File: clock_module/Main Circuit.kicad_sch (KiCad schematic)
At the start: 1 part, among them U2 NE555DR

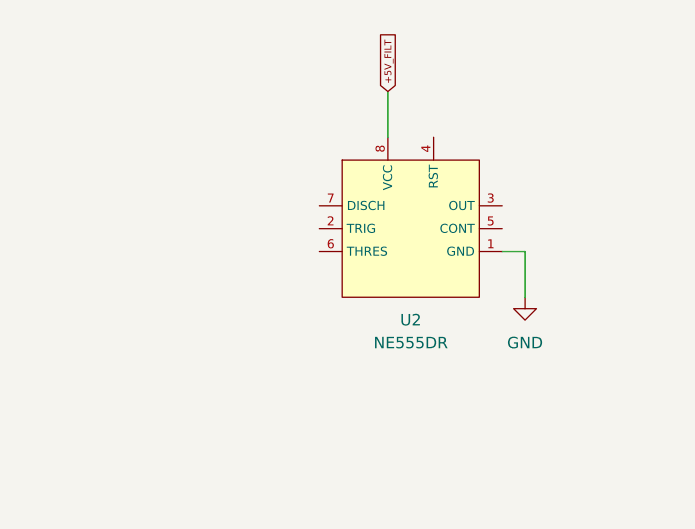
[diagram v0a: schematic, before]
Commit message: add: monostable operation circuit
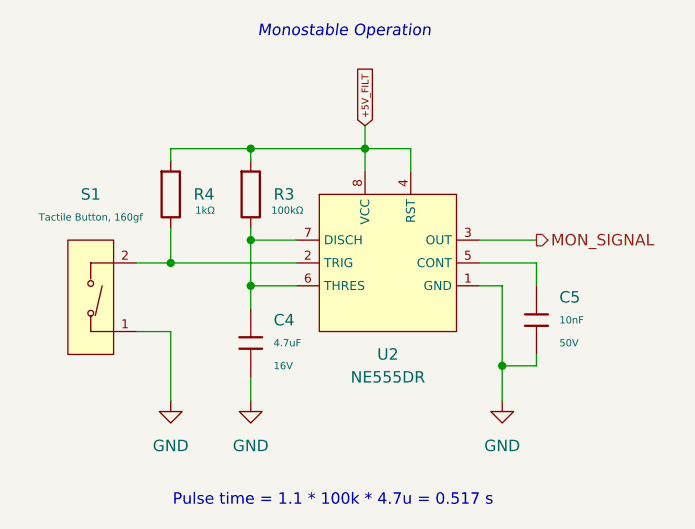
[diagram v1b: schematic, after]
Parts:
- added C4: 4.7uF, PCM_JLCPCB:C_0603, symbol PCM_JLCPCB-Capacitors:0603,4.7uF
- added C5: 10nF, PCM_JLCPCB:C_0603, symbol PCM_JLCPCB-Capacitors:0603,10nF
- added R3: 100kΩ, PCM_JLCPCB:R_0603, symbol PCM_JLCPCB-Resistors:0603,100kΩ
- added R4: 1kΩ, PCM_JLCPCB:R_0603, symbol PCM_JLCPCB-Resistors:0603,1kΩ
- added S1: Tactile Button, 160gf, PCM_JLCPCB:SW_TS-1088-AR02016, symbol PCM_JLCPCB-Connectors_Buttons:Tactile Button, 160gf, 12V, 50mA, 4.0mm
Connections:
- net +5V_FILT: now also U2.4 (RST), R3.1, R4.1
- net GND: now also C4.2, C5.2, S1.1 (A)
- net at U2.2 (TRIG): now also R4.2, S1.2 (B)
- net MON_SIGNAL: now reaches U2.3 (OUT)
- net at U2.5 (CONT): now also C5.1
- net at U2.6 (THRES): now also U2.7 (DISCH), C4.1, R3.2
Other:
- note added: "Monostable Operation"
- note added: "Pulse time = 1.1 * 100k * 4.7u = 0.517 s"
- moved on the sheet: U2

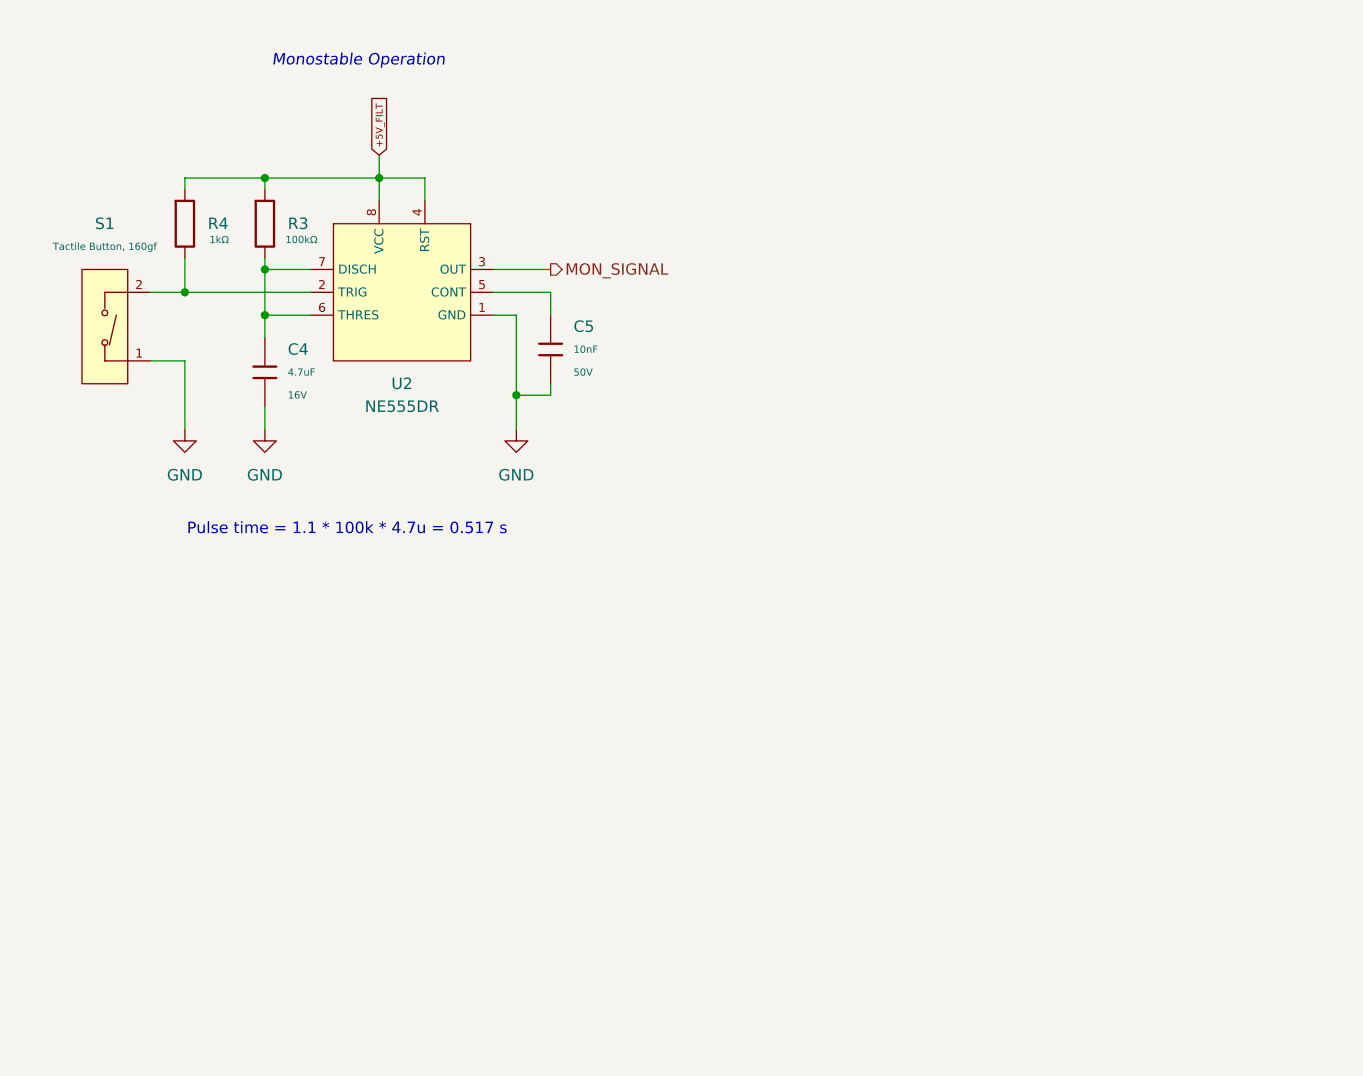
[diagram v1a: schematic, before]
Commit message: add: astable circuit
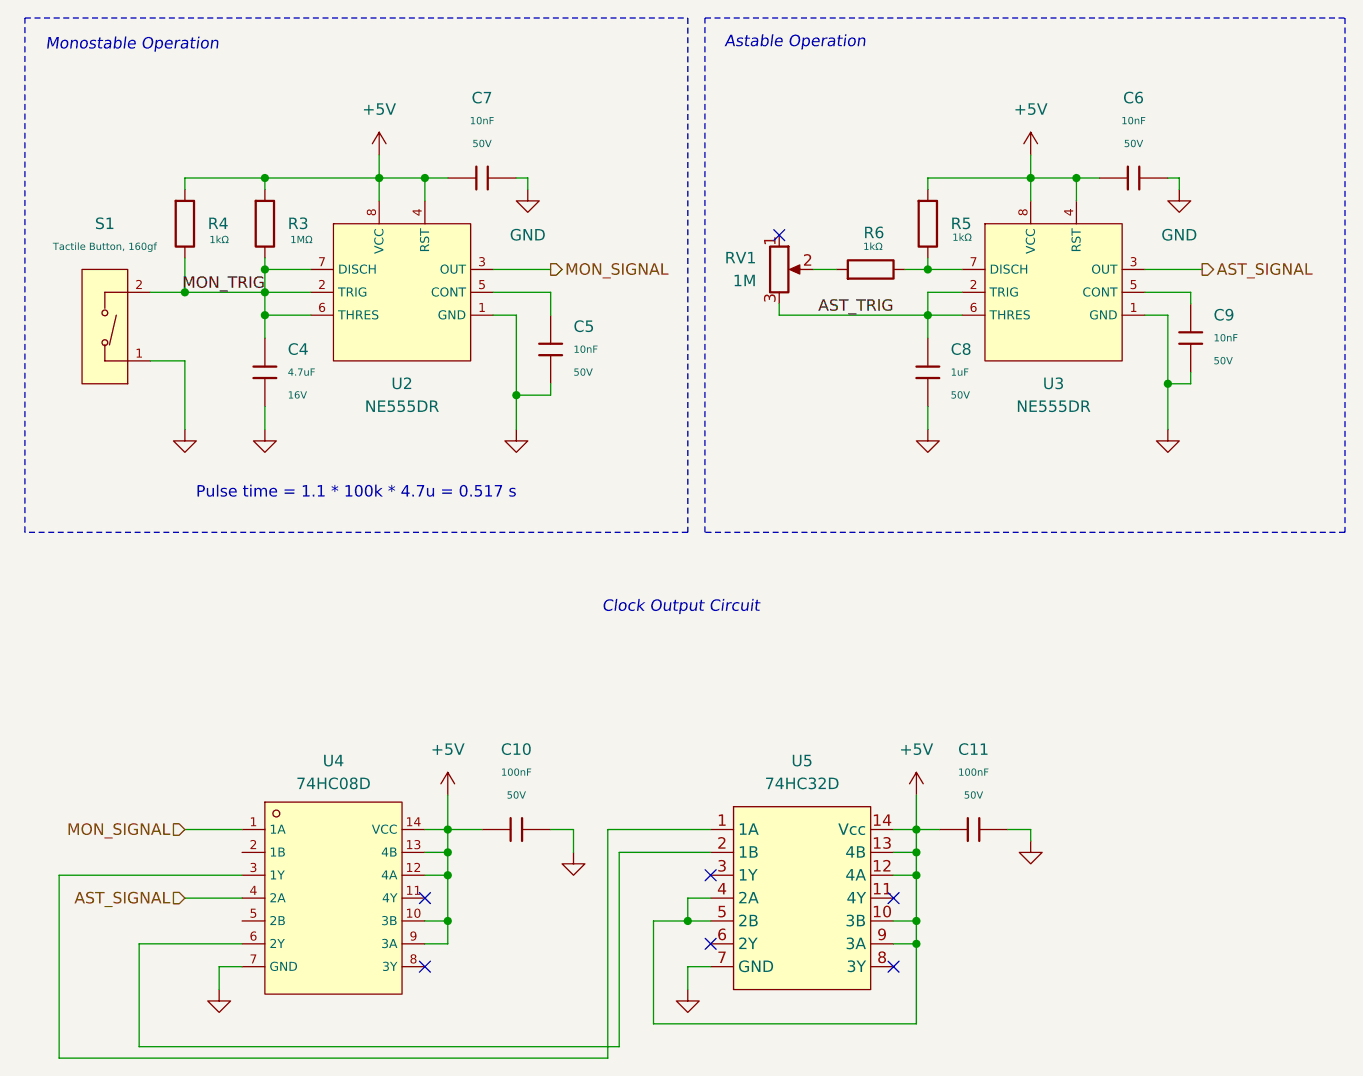
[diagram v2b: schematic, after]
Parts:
- removed R3: 100kΩ, PCM_JLCPCB:R_0603, symbol PCM_JLCPCB-Resistors:0603,100kΩ
- added C10, C11: 100nF, PCM_JLCPCB:C_0603, symbol PCM_JLCPCB-Capacitors:0603,100nF
- added C6, C7, C9: 10nF, PCM_JLCPCB:C_0603, symbol PCM_JLCPCB-Capacitors:0603,10nF
- added C8: 1uF, PCM_JLCPCB:C_0603, symbol PCM_JLCPCB-Capacitors:0603,1uF
- added R3: 1MΩ, PCM_JLCPCB:R_0603, symbol PCM_JLCPCB-Resistors:0603,1MΩ
- added R5, R6: 1kΩ, PCM_JLCPCB:R_0603, symbol PCM_JLCPCB-Resistors:0603,1kΩ
- added RV1: 1M, Potentiometer_SMD:Potentiometer_Bourns_3314G_Vertical, symbol Device:R_Potentiometer
- added U3: NE555DR, PCM_JLCPCB:SOIC-8_L4.9-W3.9-P1.27-LS6.0-BL, symbol PCM_JLCPCB-ICs:Timer, 555
- added U4: 74HC08D, PCM_JLCPCB:SOIC-14_L8.7-W3.9-P1.27-LS6.0-BL, symbol PCM_JLCPCB-ICs:Gate, AND, 4 Channel, 74HC08D,653
- added U5: 74HC32D, PCM_JLCPCB:SOIC-14_L8.7-W3.9-P1.27-LS6.0-BL, symbol PCM_JLCPCB-ICs:Gate,_OR,_4_Channel,_74HC32D,653
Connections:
- net GND: now also C10.2, C11.2, C6.2, C7.2, C8.2, C9.2, U3.1 (GND), U4.7 (GND), U5.7 (GND)
- net MON_SIGNAL: now also U4.1 (1A)
- net MON_TRIG: now reaches C4.1, U2.6 (THRES), U2.7 (DISCH)
- net MON_TRIG: now also R4.2, S1.2 (B), U2.2 (TRIG), R3.2
- net +5V_FILT renamed +5V
- net +5V: now also C10.1, C11.1, C6.1, C7.1, R3.1, R5.1, U3.4 (RST), U3.8 (VCC), U4.10 (3B), U4.12 (4A), U4.13 (4B), U4.14 (VCC), U4.9 (3A), U5.10 (3B), U5.12 (4A), U5.13 (4B), U5.14 (Vcc), U5.4 (2A), U5.5 (2B), U5.9 (3A)
- new net: C9.1, U3.5 (CONT)
- new net: R5.2, R6.2, U3.7 (DISCH)
- new net: U4.3 (1Y), U5.1 (1A)
- new net: U4.6 (2Y), U5.2 (1B)
- new net: R6.1, RV1.2
- new net AST_SIGNAL: U3.3 (OUT), U4.4 (2A)
- new net AST_TRIG: C8.1, RV1.3, U3.2 (TRIG), U3.6 (THRES)
- no-connect marks 0 -> 7
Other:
- note added: "Astable Operation"
- note added: "Clock Output Circuit"

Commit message: pcb routes (unfinished)
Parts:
- added C12, C13: 10nF, PCM_JLCPCB:C_0603, symbol PCM_JLCPCB-Capacitors:0603,10nF
- added C14: 100nF, PCM_JLCPCB:C_0603, symbol PCM_JLCPCB-Capacitors:0603,100nF
- added D1: Yellow, PCM_JLCPCB:D_0603, symbol PCM_JLCPCB-Diodes:LED,0603,Yellow
- added J2: Conn_01x03, Connector_PinHeader_2.54mm:PinHeader_1x03_P2.54mm_Vertical, symbol Connector_Generic:Conn_01x03
- added R7: 220Ω, PCM_JLCPCB:R_0603, symbol PCM_JLCPCB-Resistors:0603,220Ω
- added R8, R9: 1kΩ, PCM_JLCPCB:R_0603, symbol PCM_JLCPCB-Resistors:0603,1kΩ
- added SW1: SW_SPDT, Buttons_THT:SW_SPDT_L7.0mm_H16.0mm_W7.00mm, symbol Switch:SW_SPDT
- added U6: NE555DR, PCM_JLCPCB:SOIC-8_L4.9-W3.9-P1.27-LS6.0-BL, symbol PCM_JLCPCB-ICs:Timer, 555
- added U7: 74HC04D, PCM_JLCPCB:SOIC-14_L8.7-W3.9-P1.27-LS6.0-BL, symbol PCM_JLCPCB-ICs:Inverter, 6 Channel, 74HC04D,653
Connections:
- net +5V: now also C12.1, C14.1, R8.1, R9.1, U6.8 (VCC), U7.11 (5A), U7.13 (6A), U7.14 (VCC), U7.9 (4A); no longer U4.10 (3B), U4.9 (3A)
- net GND: now also C12.2, C13.2, C14.2, R7.1, SW1.2 (B), U6.1 (GND), U6.6 (THRES), U7.7 (GND)
- net SIG_SELECT: now reaches U4.2 (1B)
- net SIG_SELECT: now also U6.3 (OUT), U7.1 (1A)
- net !SIG_SELECT: now reaches U4.5 (2B)
- net !SIG_SELECT: now also U7.2 (1Y)
- net CLK_SIGNAL: now reaches U4.8 (3Y)
- net CLK_SIGNAL: now also D1.2, J2.2 (Pin_2), U7.5 (3A)
- net at U5.3 (1Y): now also U4.10 (3B)
- new net: C13.1, U6.5 (CONT)
- new net: U4.9 (3A), U7.4 (2Y)
- new net: R8.2, SW1.1 (A), U6.2 (TRIG)
- new net: R9.2, SW1.3 (C), U6.4 (RST)
- new net: D1.1, R7.2
- new net !CLK_SIGNAL: J2.3 (Pin_3), U7.6 (3Y)
- new net HLT: J2.1 (Pin_1), U7.3 (2A)
- no-connect marks 7 -> 9
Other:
- note added: "!CLK - Inverted Clock Signal"
- note added: "Bistable Operation"
- note added: "CLK - Clock Signal"
- note added: "HLT - From Controller Circuit"
- note added: "Input/Output Headers"
- note added: "Pulse time = 1.1 * 1M * 4.7u = 5.17 s"
- note removed: "Pulse time = 1.1 * 100k * 4.7u = 0.517 s"
- moved on the sheet: C6, C8, C9, R5, R6, RV1, U3

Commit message: finished board
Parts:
- RV1: LCSC (none) -> C780218
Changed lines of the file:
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@@
+			)
+		)
+		(property "LCSC" "C780218"
+			(at 110.49 45.72 0)
+			(effects
+				(font
+					(size 1.27 1.27)
+				)
+				(hide yes)
 			)
 		)

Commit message: final v1.0.0 project
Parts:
- removed J2: Conn_01x03, Connector_PinHeader_2.54mm:PinHeader_1x03_P2.54mm_Vertical, symbol Connector_Generic:Conn_01x03
- removed R6: 1kΩ, PCM_JLCPCB:R_0603, symbol PCM_JLCPCB-Resistors:0603,1kΩ
- added J3: Conn_01x05, Connector_PinHeader_2.54mm:PinHeader_1x05_P2.54mm_Vertical, symbol Connector_Generic:Conn_01x05
- added R6: 200kΩ, PCM_JLCPCB:R_0603, symbol PCM_JLCPCB-Resistors:0603,200kΩ
- RV1: value 1M -> 200k; LCSC C780218 -> C3345207
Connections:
- net !CLK_SIGNAL: now also J3.3 (Pin_3)
- net +5V: now also J3.4 (Pin_4)
- net CLK_SIGNAL: now also J3.2 (Pin_2)
- net GND: now also J3.5 (Pin_5)
- net HLT: now also J3.1 (Pin_1)
- net at R5.2, U3.7 (DISCH): now also R6.2
- net at RV1.2: now also R6.1
